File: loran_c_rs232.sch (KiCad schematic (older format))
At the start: 30 parts, among them P301 UART1 3V3, P302 DB9 Ribbon 1, P303 DB9 Ribbon 2, U301 ST3232, U302 ST3232, U303 ST3232

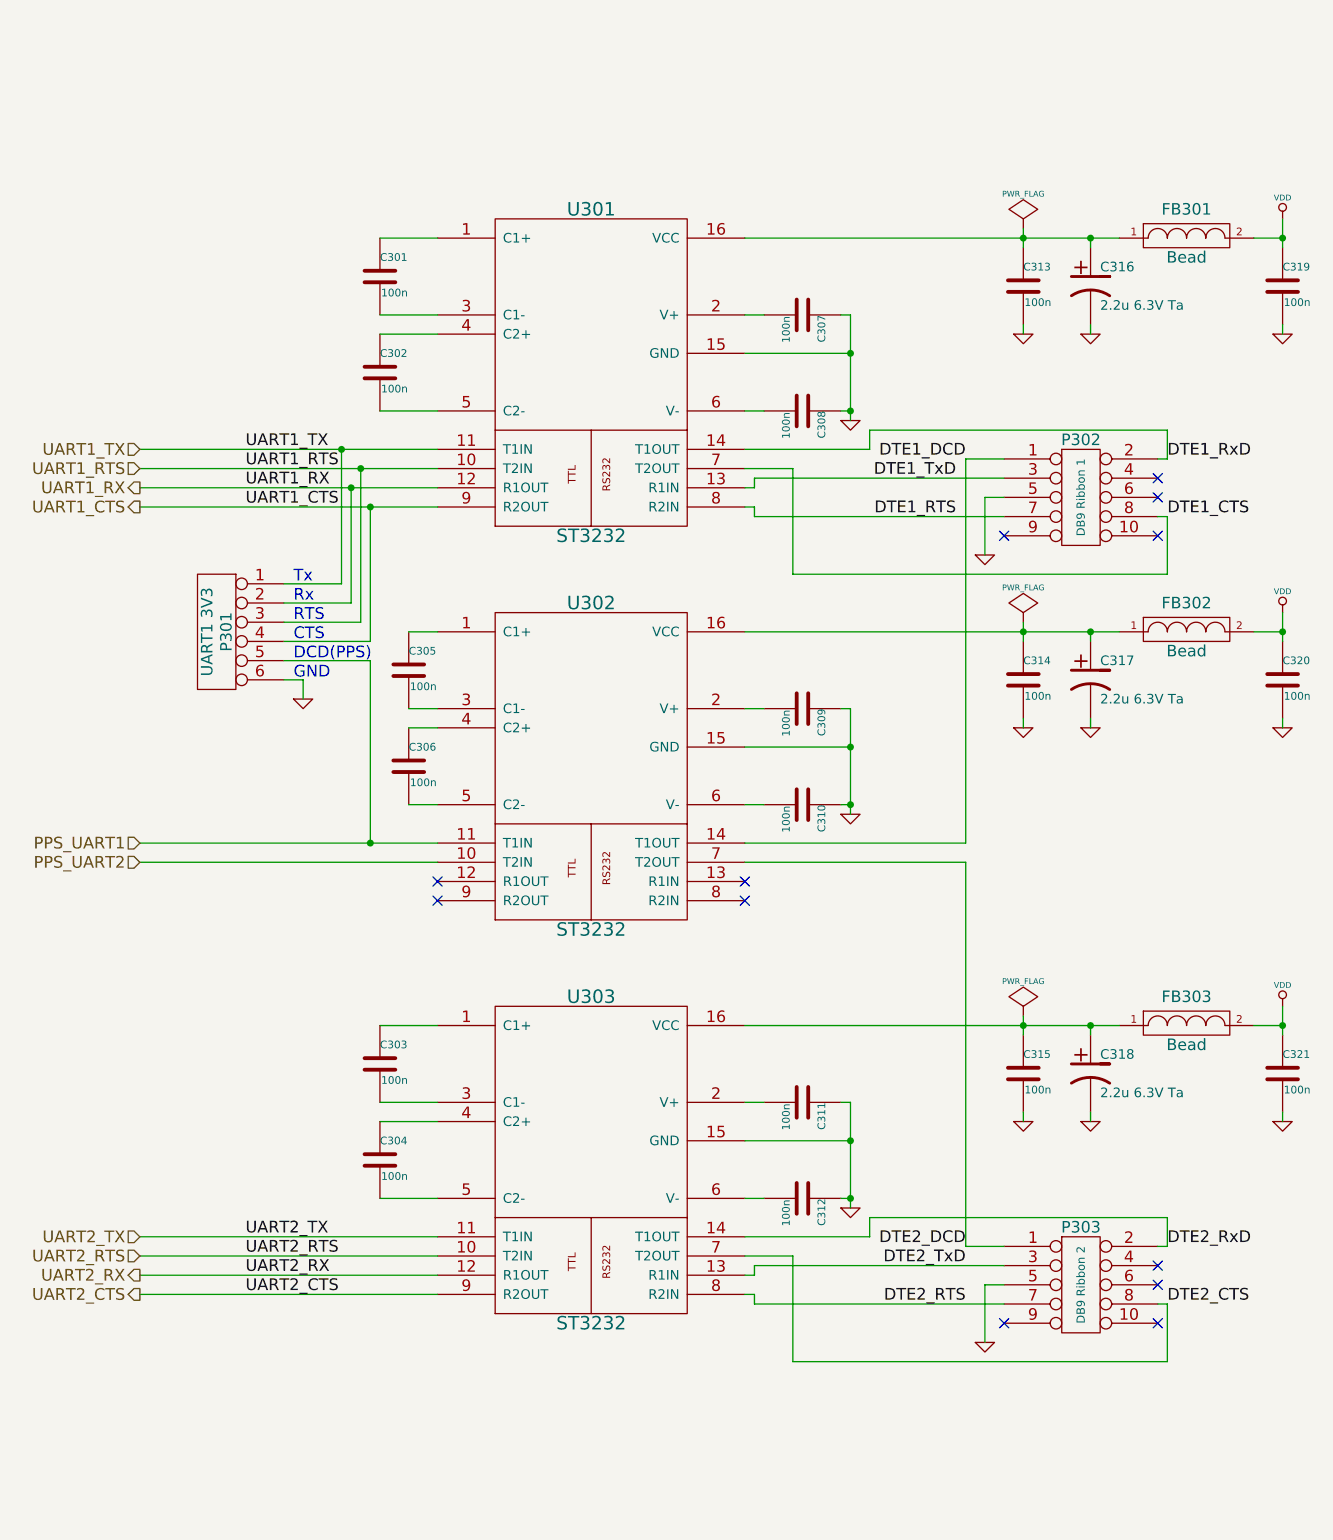
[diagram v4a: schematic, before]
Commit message: Update: minor schematic rework (due to PCB routing), PCB routing in early stage
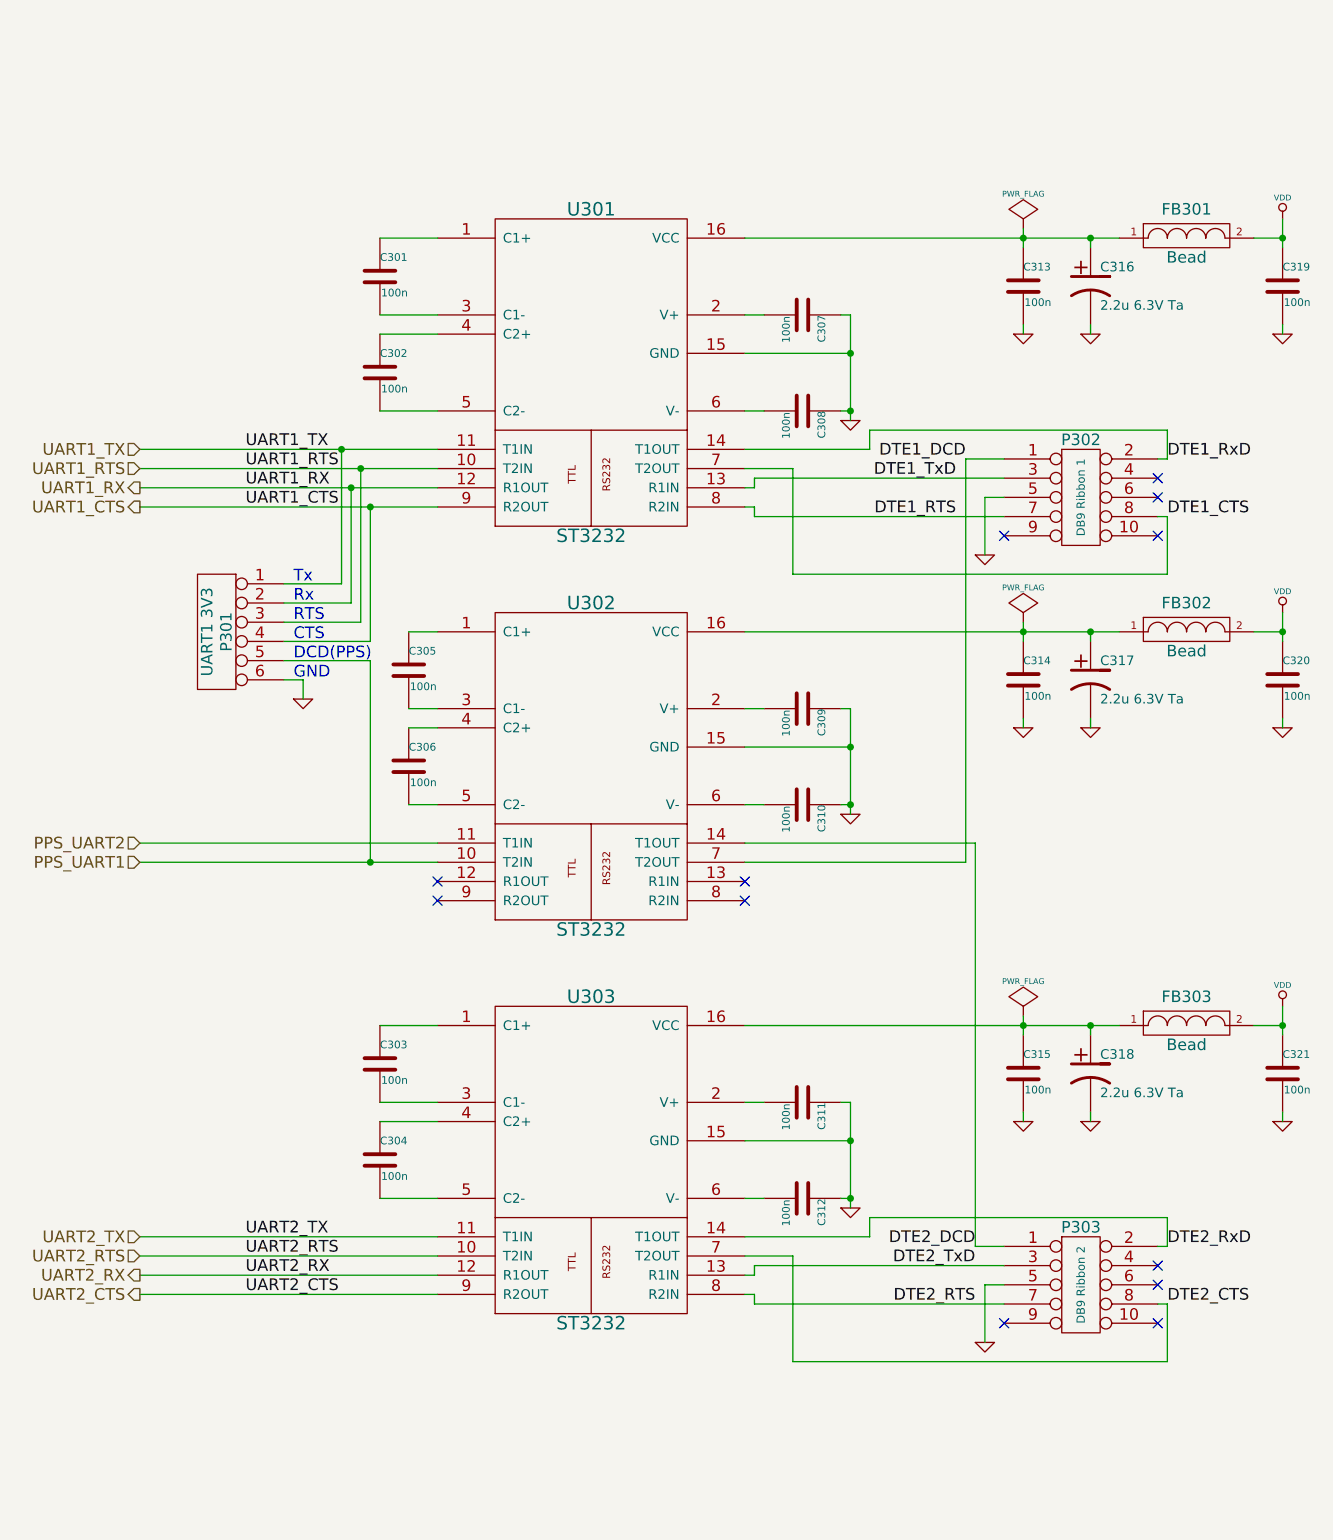
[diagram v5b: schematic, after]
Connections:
- net DTE1_DCD: now also U302.7 (T2OUT); no longer U302.14 (T1OUT)
- net DTE2_DCD: now also U302.14 (T1OUT); no longer U302.7 (T2OUT)
- net PPS_UART1: now also U302.10 (T2IN); no longer U302.11 (T1IN)
- net PPS_UART2: now also U302.11 (T1IN); no longer U302.10 (T2IN)
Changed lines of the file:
@@
 	1    0    0    -1
 $EndComp
-Text Label 5500 7250 2    61   ~ 0
+Text Label 5550 7250 2    61   ~ 0
 DTE2_DCD
-Text Label 5500 7350 2    61   ~ 0
+Text Label 5550 7350 2    61   ~ 0
 DTE2_TxD
-Text Label 5500 7550 2    61   ~ 0
+Text Label 5550 7550 2    61   ~ 0
 DTE2_RTS
 Text Label 6550 7250 0    61   ~ 0
@@
 DTE2_CTS
 $Comp
-L GND #PWR037
+L GND #PWR057
 U 1 1 52DBAE37
 P 5600 7750
-F 0 "#PWR037" H 5600 7750 30  0001 C CNN
+F 0 "#PWR057" H 5600 7750 30  0001 C CNN
 F 1 "GND" H 5600 7680 30  0001 C CNN
 F 2 "" H 5600 7750 60  0000 C CNN
@@
 DTE1_CTS
 $Comp
-L GND #PWR038
+L GND #PWR058
 U 1 1 52DBB093
 P 5600 3650
-F 0 "#PWR038" H 5600 3650 30  0001 C CNN
+F 0 "#PWR058" H 5600 3650 30  0001 C CNN
 F 1 "GND" H 5600 3580 30  0001 C CNN
 F 2 "" H 5600 3650 60  0000 C CNN
@@
 $EndComp
 $Comp
-L GND #PWR039
+L GND #PWR059
 U 1 1 52DBC5A6
 P 4900 2950
-F 0 "#PWR039" H 4900 2950 30  0001 C CNN
+F 0 "#PWR059" H 4900 2950 30  0001 C CNN
 F 1 "GND" H 4900 2880 30  0001 C CNN
 F 2 "" H 4900 2950 60  0000 C CNN
@@
 	4600 3200 4600 3750
 Wire Wire Line
-	6550 3750 4600 3750
-Wire Wire Line
-	6550 3450 6550 3750
+	4600 3750 6550 3750
+Wire Wire Line
+	6550 3750 6550 3450
 $Comp
 L MAX232 U303
@@
 $EndComp
 $Comp
-L GND #PWR040
+L GND #PWR060
 U 1 1 52DBD4A5
 P 4900 7050
-F 0 "#PWR040" H 4900 7050 30  0001 C CNN
+F 0 "#PWR060" H 4900 7050 30  0001 C CNN
 F 1 "GND" H 4900 6980 30  0001 C CNN
 F 2 "" H 4900 7050 60  0000 C CNN
@@
 $EndComp
 $Comp
-L GND #PWR041
+L GND #PWR061
 U 1 1 52DBD9EF
 P 4900 5000
-F 0 "#PWR041" H 4900 5000 30  0001 C CNN
+F 0 "#PWR061" H 4900 5000 30  0001 C CNN
 F 1 "GND" H 4900 4930 30  0001 C CNN
 F 2 "" H 4900 5000 60  0000 C CNN
@@
 	2600 4950 2750 4950
 Wire Wire Line
-	4350 5150 5500 5150
-Wire Wire Line
-	4350 5250 5500 5250
-Wire Wire Line
-	5500 5150 5500 3150
+	5500 3150 5500 5250
 Wire Wire Line
 	5500 3150 5700 3150
-Wire Wire Line
-	5500 5250 5500 7250
-Wire Wire Line
-	5500 7250 5700 7250
 Wire Wire Line
 	1200 3100 2750 3100
@@
 $EndComp
 $Comp
-L GND #PWR042
+L GND #PWR062
 U 1 1 52DC08D0
 P 5800 2500
-F 0 "#PWR042" H 5800 2500 30  0001 C CNN
+F 0 "#PWR062" H 5800 2500 30  0001 C CNN
 F 1 "GND" H 5800 2430 30  0001 C CNN
 F 2 "" H 5800 2500 60  0000 C CNN
@@
 $EndComp
 $Comp
-L GND #PWR043
+L GND #PWR063
 U 1 1 52DC08DB
 P 6150 2500
-F 0 "#PWR043" H 6150 2500 30  0001 C CNN
+F 0 "#PWR063" H 6150 2500 30  0001 C CNN
 F 1 "GND" H 6150 2430 30  0001 C CNN
 F 2 "" H 6150 2500 60  0000 C CNN
@@
 $EndComp
 $Comp
-L GND #PWR044
+L GND #PWR064
 U 1 1 52DC0F53
 P 7150 2500
-F 0 "#PWR044" H 7150 2500 30  0001 C CNN
+F 0 "#PWR064" H 7150 2500 30  0001 C CNN
 F 1 "GND" H 7150 2430 30  0001 C CNN
 F 2 "" H 7150 2500 60  0000 C CNN
@@
 Connection ~ 7150 2000
 $Comp
-L VDD #PWR045
+L VDD #PWR065
 U 1 1 52DC1066
 P 7150 1900
-F 0 "#PWR045" H 7150 2000 30  0001 C CNN
+F 0 "#PWR065" H 7150 2000 30  0001 C CNN
 F 1 "VDD" H 7150 2010 30  0000 C CNN
 F 2 "" H 7150 1900 60  0000 C CNN
@@
 $EndComp
 $Comp
-L GND #PWR046
+L GND #PWR066
 U 1 1 52DC12C1
 P 5800 4550
-F 0 "#PWR046" H 5800 4550 30  0001 C CNN
+F 0 "#PWR066" H 5800 4550 30  0001 C CNN
 F 1 "GND" H 5800 4480 30  0001 C CNN
 F 2 "" H 5800 4550 60  0000 C CNN
@@
 $EndComp
 $Comp
-L GND #PWR047
+L GND #PWR067
 U 1 1 52DC12C7
 P 6150 4550
-F 0 "#PWR047" H 6150 4550 30  0001 C CNN
+F 0 "#PWR067" H 6150 4550 30  0001 C CNN
 F 1 "GND" H 6150 4480 30  0001 C CNN
 F 2 "" H 6150 4550 60  0000 C CNN
@@
 $EndComp
 $Comp
-L GND #PWR048
+L GND #PWR068
 U 1 1 52DC12DF
 P 7150 4550
-F 0 "#PWR048" H 7150 4550 30  0001 C CNN
+F 0 "#PWR068" H 7150 4550 30  0001 C CNN
 F 1 "GND" H 7150 4480 30  0001 C CNN
 F 2 "" H 7150 4550 60  0000 C CNN
@@
 Connection ~ 7150 4050
 $Comp
-L VDD #PWR049
+L VDD #PWR069
 U 1 1 52DC12EA
 P 7150 3950
-F 0 "#PWR049" H 7150 4050 30  0001 C CNN
+F 0 "#PWR069" H 7150 4050 30  0001 C CNN
 F 1 "VDD" H 7150 4060 30  0000 C CNN
 F 2 "" H 7150 3950 60  0000 C CNN
@@
 $EndComp
 $Comp
-L GND #PWR050
+L GND #PWR070
 U 1 1 52DC12FF
 P 5800 6600
-F 0 "#PWR050" H 5800 6600 30  0001 C CNN
+F 0 "#PWR070" H 5800 6600 30  0001 C CNN
 F 1 "GND" H 5800 6530 30  0001 C CNN
 F 2 "" H 5800 6600 60  0000 C CNN
@@
 $EndComp
 $Comp
-L GND #PWR051
+L GND #PWR071
 U 1 1 52DC1305
 P 6150 6600
-F 0 "#PWR051" H 6150 6600 30  0001 C CNN
+F 0 "#PWR071" H 6150 6600 30  0001 C CNN
 F 1 "GND" H 6150 6530 30  0001 C CNN
 F 2 "" H 6150 6600 60  0000 C CNN
@@
 $EndComp
 $Comp
-L GND #PWR052
+L GND #PWR072
 U 1 1 52DC131D
 P 7150 6600
-F 0 "#PWR052" H 7150 6600 30  0001 C CNN
+F 0 "#PWR072" H 7150 6600 30  0001 C CNN
 F 1 "GND" H 7150 6530 30  0001 C CNN
 F 2 "" H 7150 6600 60  0000 C CNN
@@
 Connection ~ 7150 6100
 $Comp
-L VDD #PWR053
+L VDD #PWR073
 U 1 1 52DC1328
 P 7150 6000
-F 0 "#PWR053" H 7150 6100 30  0001 C CNN
+F 0 "#PWR073" H 7150 6100 30  0001 C CNN
 F 1 "VDD" H 7150 6110 30  0000 C CNN
 F 2 "" H 7150 6000 60  0000 C CNN
@@
 Wire Wire Line
 	1950 4200 2400 4200
-Wire Wire Line
-	2400 4200 2400 5150
-Connection ~ 2400 5150
+Connection ~ 2400 5250
 Wire Wire Line
 	1950 4300 2050 4300
@@
 	2050 4300 2050 4400
 $Comp
-L GND #PWR054
+L GND #PWR074
 U 1 1 52DC2978
 P 2050 4400
-F 0 "#PWR054" H 2050 4400 30  0001 C CNN
+F 0 "#PWR074" H 2050 4400 30  0001 C CNN
 F 1 "GND" H 2050 4330 30  0001 C CNN
 F 2 "" H 2050 4400 60  0000 C CNN
@@
 Text HLabel 1200 3400 0    61   Output ~ 0
 UART1_CTS
+Text HLabel 1200 5250 0    61   Input ~ 0
+PPS_UART1
 Text HLabel 1200 5150 0    61   Input ~ 0
-PPS_UART1
-Text HLabel 1200 5250 0    61   Input ~ 0
 PPS_UART2
 Text HLabel 1200 7200 0    61   Input ~ 0
@@
 UART2_CTS
 $Comp
-L PWR_FLAG #FLG055
+L PWR_FLAG #FLG075
 U 1 1 52E7FFCD
 P 5800 1950
-F 0 "#FLG055" H 5800 2045 30  0001 C CNN
+F 0 "#FLG075" H 5800 2045 30  0001 C CNN
 F 1 "PWR_FLAG" H 5800 2130 30  0000 C CNN
 F 2 "" H 5800 1950 60  0000 C CNN
@@
 $EndComp
 $Comp
-L PWR_FLAG #FLG056
+L PWR_FLAG #FLG076
 U 1 1 52E80075
 P 5800 4000
-F 0 "#FLG056" H 5800 4095 30  0001 C CNN
+F 0 "#FLG076" H 5800 4095 30  0001 C CNN
 F 1 "PWR_FLAG" H 5800 4180 30  0000 C CNN
 F 2 "" H 5800 4000 60  0000 C CNN
@@
 $EndComp
 $Comp
-L PWR_FLAG #FLG057
+L PWR_FLAG #FLG077
 U 1 1 52E8010C
 P 5800 6050
-F 0 "#FLG057" H 5800 6145 30  0001 C CNN
+F 0 "#FLG077" H 5800 6145 30  0001 C CNN
 F 1 "PWR_FLAG" H 5800 6230 30  0000 C CNN
 F 2 "" H 5800 6050 60  0000 C CNN
@@
 	6550 3450 6500 3450
 NoConn ~ 6500 3550
+Wire Wire Line
+	2400 4200 2400 5250
+Wire Wire Line
+	5500 5250 4350 5250
+Wire Wire Line
+	4350 5150 5550 5150
+Wire Wire Line
+	5550 5150 5550 7250
+Wire Wire Line
+	5550 7250 5700 7250
 $EndSCHEMATC
